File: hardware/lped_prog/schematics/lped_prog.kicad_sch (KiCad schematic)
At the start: 12 parts, among them J1 J-Link Header, J2 Conn_01x01_Pin, J3 Conn_01x01_Pin, J4 Conn_01x01_Pin, J5 Conn_01x01_Pin, J6 Conn_01x01_Pin, J7 Conn_01x01_Pin

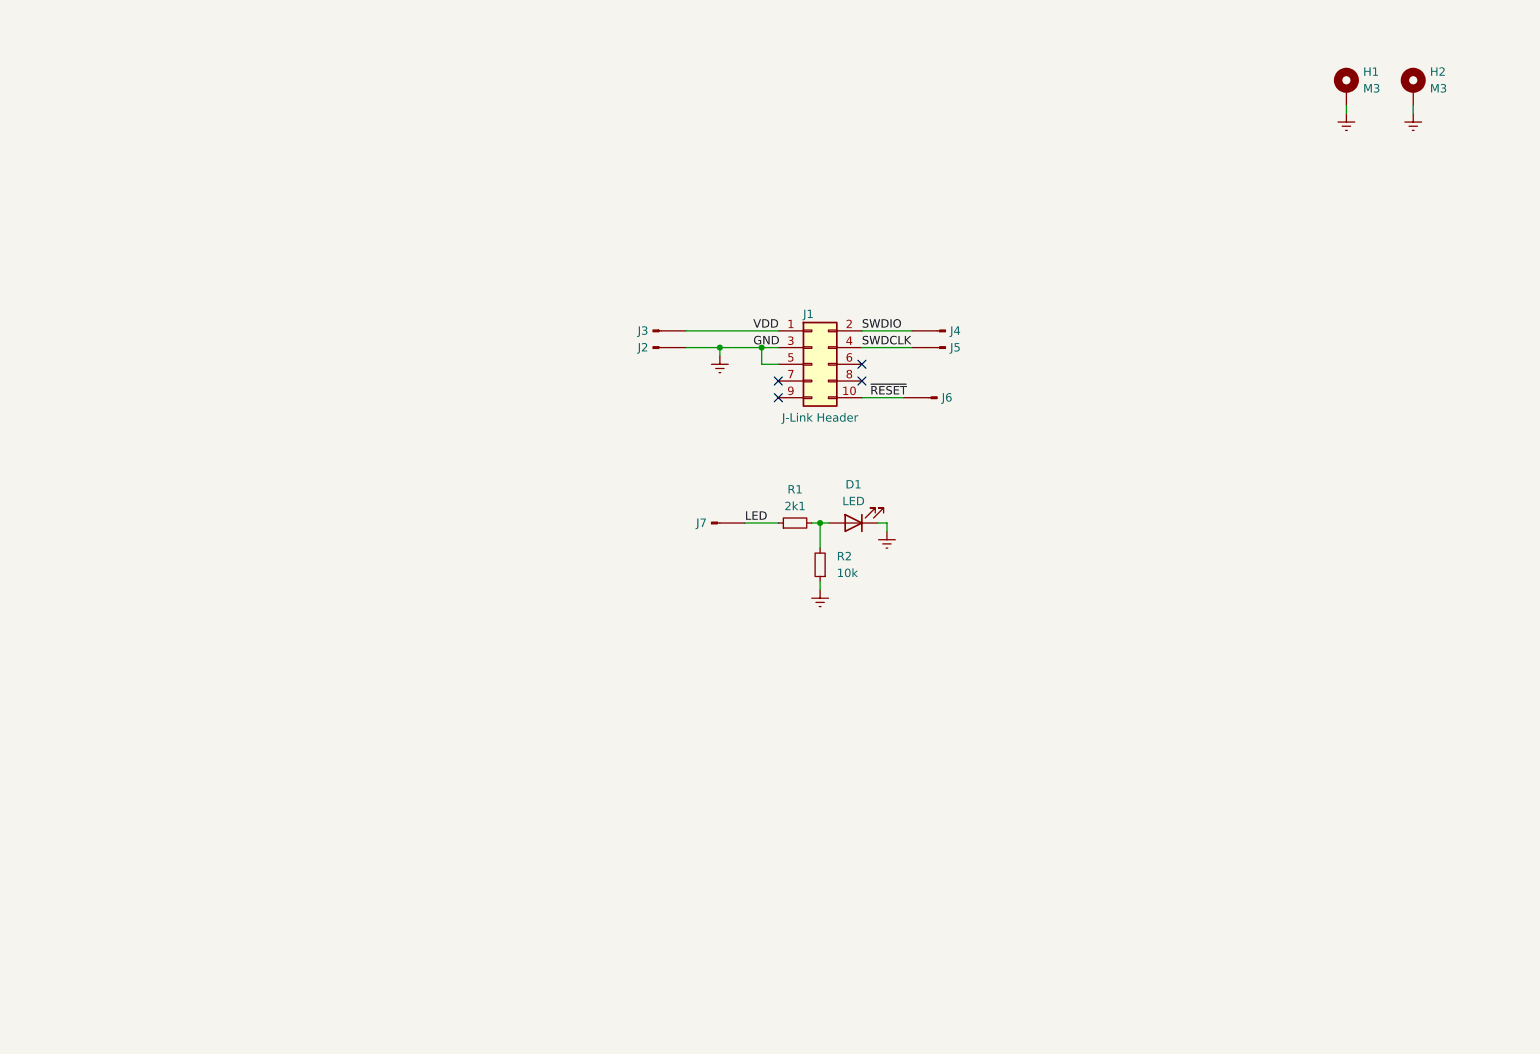
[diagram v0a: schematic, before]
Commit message: feat(hardware): added usb and manual input to programmer, added reset button and connection switch
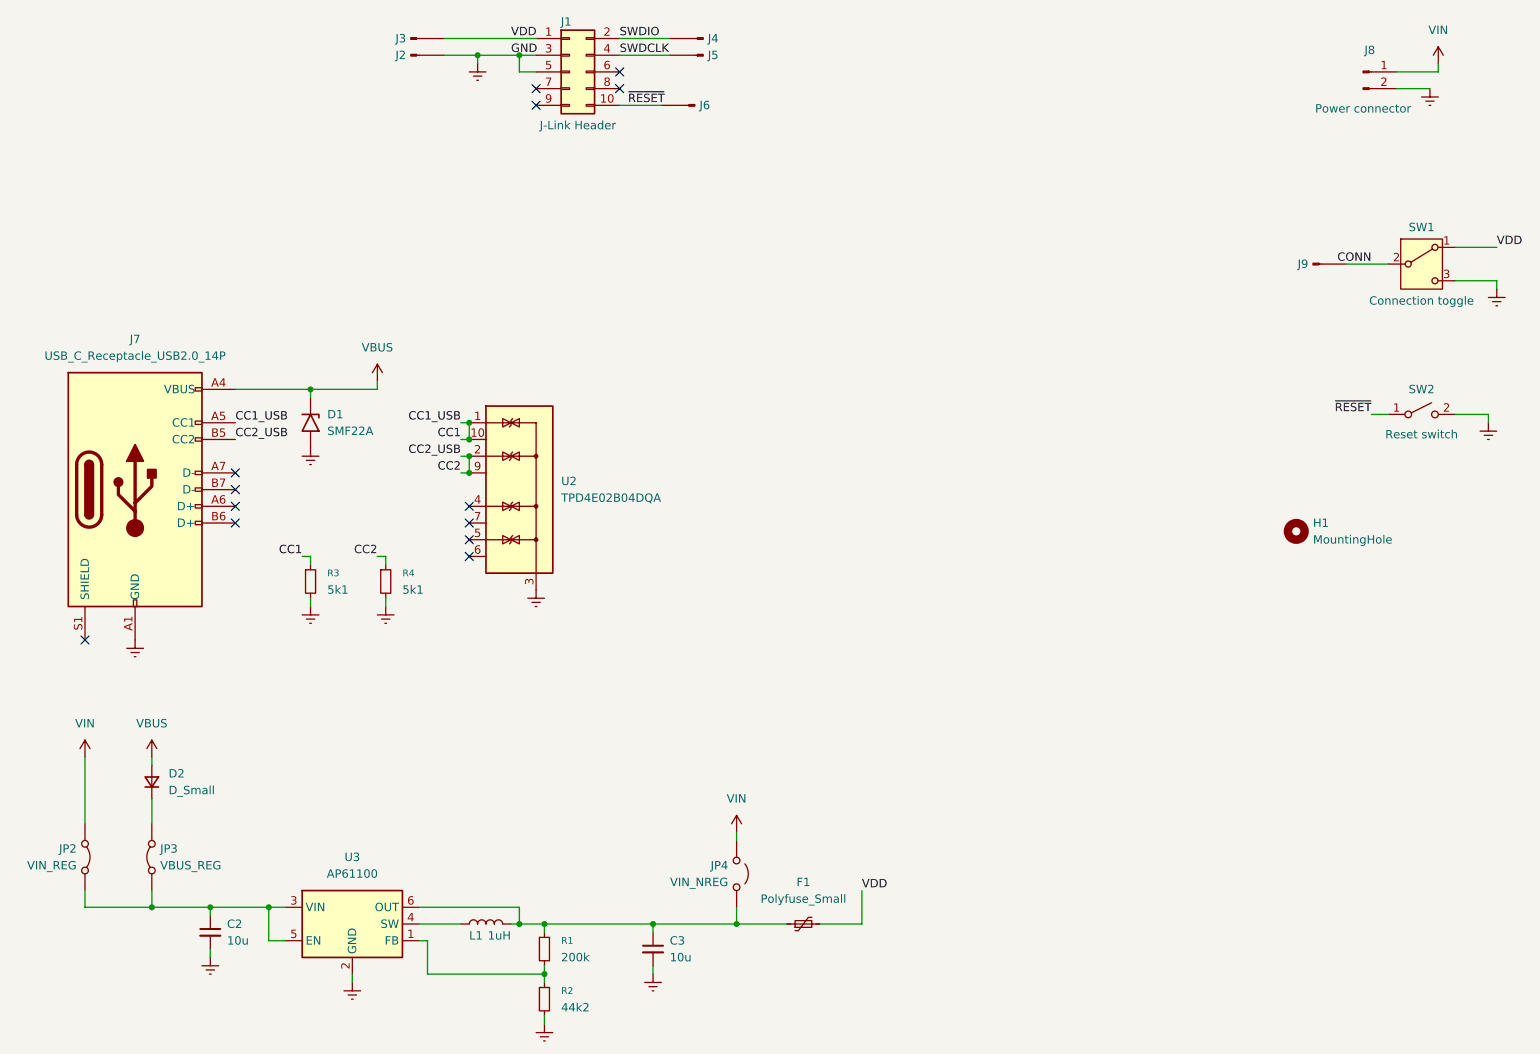
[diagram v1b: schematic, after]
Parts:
- removed D1: LED, Diode_SMD:D_0805_2012Metric, symbol Device:LED
- removed H1, H2: M3, MountingHole:MountingHole_2.7mm_M2.5_ISO7380_Pad, symbol Mechanical:MountingHole_Pad
- removed J7: Conn_01x01_Pin, Connector_Pin:Pin_D0.9mm_L10.0mm_W2.4mm_FlatFork, symbol Connector:Conn_01x01_Pin
- added C2, C3: 10u, Capacitor_SMD:C_0603_1608Metric, symbol Device:C_Small
- added D1: SMF22A, Diode_SMD:D_SMF, symbol Diode:SMF22A
- added D2: D_Small, Diode_SMD:D_0402_1005Metric, symbol Device:D_Small
- added F1: Polyfuse_Small, Fuse:Fuse_1206_3216Metric, symbol Device:Polyfuse_Small
- added H1: MountingHole, MountingHole:MountingHole_3.2mm_M3, symbol Mechanical:MountingHole
- added J7: USB_C_Receptacle_USB2.0_14P, Connector_USB:USB_C_Receptacle_GCT_USB4105-xx-A_16P_TopMnt_Horizontal, symbol Connector:USB_C_Receptacle_USB2.0_14P
- added J8: Power connector, Connector_PinHeader_2.54mm:PinHeader_1x02_P2.54mm_Vertical, symbol Connector:Conn_01x02_Pin
- added J9: Conn_01x01_Pin, Connector_Pin:Pin_D0.9mm_L10.0mm_W2.4mm_FlatFork, symbol Connector:Conn_01x01_Pin
- added JP2: VIN_REG, Connector_PinHeader_2.54mm:PinHeader_1x02_P2.54mm_Vertical, symbol Jumper:Jumper_2_Bridged
- added JP3: VBUS_REG, Connector_PinHeader_2.54mm:PinHeader_1x02_P2.54mm_Vertical, symbol Jumper:Jumper_2_Bridged
- added JP4: VIN_NREG, Connector_PinHeader_2.54mm:PinHeader_1x02_P2.54mm_Vertical, symbol Jumper:Jumper_2_Open
- added L1: 1uH, Inductor_SMD:L_0805_2012Metric, symbol Device:L
- added R3, R4: 5k1, Resistor_SMD:R_0402_1005Metric, symbol Device:R_Small
- added SW1: Connection toggle, Switches_Toggles:EG1215AA, symbol Switch:SW_SPDT
- added SW2: Reset switch, Button_Switch_THT:SW_PUSH_6mm_H4.3mm, symbol Switch:SW_SPST
- added U2: TPD4E02B04DQA, Package_SON:USON-10_2.5x1.0mm_P0.5mm, symbol Power_Protection:TPD4E02B04DQA
- added U3: AP61100, Package_TO_SOT_SMD:SOT-563, symbol Regulator_Switching:AP61300Z6
- R1: value 2k1 -> 200k
- R2: value 10k -> 44k2
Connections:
- net Earth: now also R2.2, C2.2, C3.2, D1.2 (A2), J7.A1 (GND), J7.A12 (GND), J7.B1 (GND), J7.B12 (GND), J8.2 (Pin_2), R3.2, R4.2, SW1.3 (C), SW2.2 (B), U2.3 (G), U2.8 (G), U3.2 (GND); no longer R2.1
- net VDD: now also F1.2, SW1.1 (A)
- net ~{RESET}: now also SW2.1 (A)
- net at R1.2: now also R2.1, U3.1 (FB); no longer R2.2
- net LED: no longer names the net of R1.1
- net LED: now also C3.1, F1.1, JP4.1 (A), L1.2, U3.6 (OUT)
- new net: C2.1, JP2.1 (A), JP3.1 (A), U3.3 (VIN), U3.5 (EN)
- new net: D2.1 (K), JP3.2 (B)
- new net: L1.1, U3.4 (SW)
- new net CC1: J7.A5 (CC1), R3.1, U2.1 (IO1), U2.10 (NC)
- new net CC2: J7.B5 (CC2), R4.1, U2.2 (IO2), U2.9 (NC)
- new net CONN: J9.1 (Pin_1), SW1.2 (B)
- new net VBUS: D1.1 (A1), D2.2 (A), J7.A4 (VBUS), J7.A9 (VBUS), J7.B4 (VBUS), J7.B9 (VBUS)
- new net VIN: J8.1 (Pin_1), JP2.2 (B), JP4.2 (B)
- no-connect marks 4 -> 13
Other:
- moved on the sheet: J1, J2, J3, J4, J5, J6

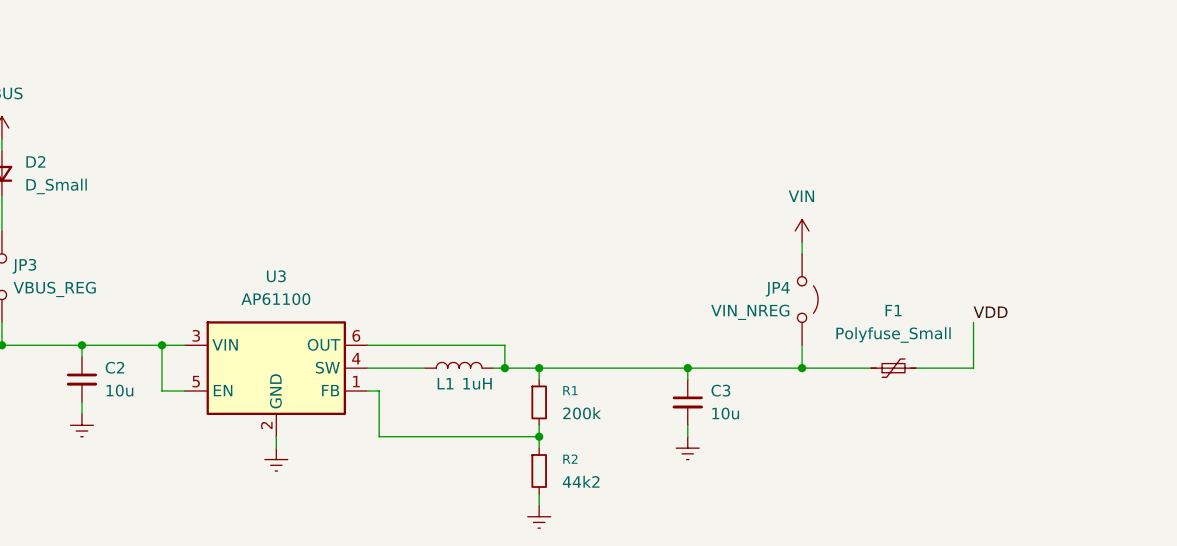
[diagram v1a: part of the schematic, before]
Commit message: feat(hardware): chaged regulator
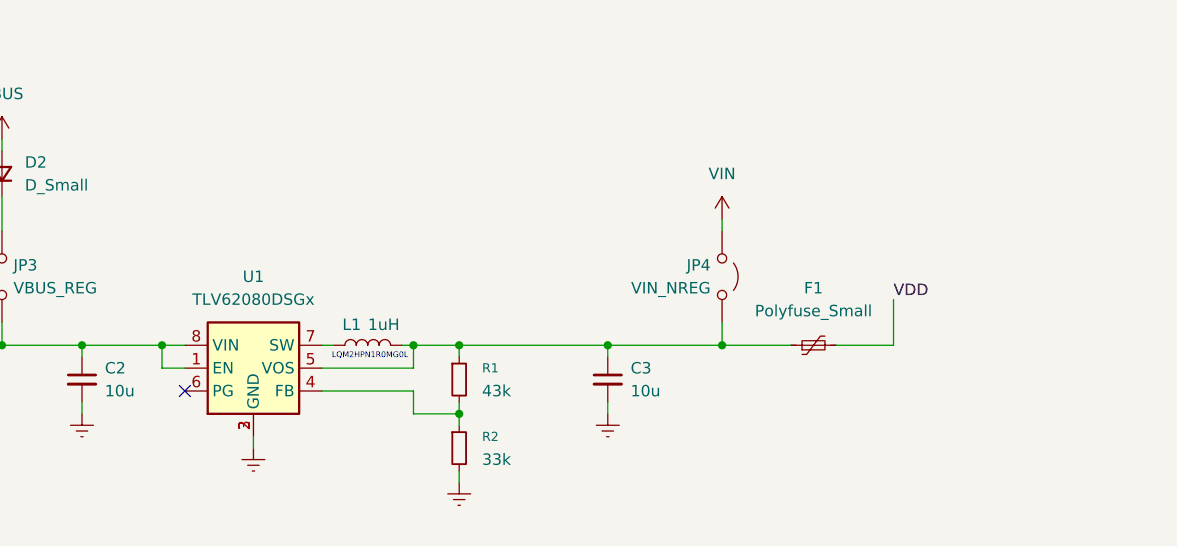
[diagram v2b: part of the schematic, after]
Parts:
- removed U3: AP61100, Package_TO_SOT_SMD:SOT-563, symbol Regulator_Switching:AP61300Z6
- added U1: TLV62080DSGx, Package_SON:WSON-8-1EP_2x2mm_P0.5mm_EP0.9x1.6mm, symbol Regulator_Switching:TLV62080DSGx
- L1: footprint Inductor_SMD:L_0805_2012Metric -> Inductor_SMD:L_1008_2520Metric
- R1: value 200k -> 43k
- R2: value 44k2 -> 33k
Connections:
- net Earth: now also U1.2 (GND), U1.3 (GND), U1.9 (GND)
- net at C3.1, F1.1, JP4.1 (A)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: now also U1.5 (VOS)
- net at R1.2, R2.1: now also U1.4 (FB)
- net at C2.1, JP2.1 (A), JP3.1 (A): now also U1.1 (EN), U1.8 (VIN)
- net at L1.1: now also U1.7 (SW)
- no-connect marks 13 -> 14
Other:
- note added: "LQM2HPN1R0MG0L"
- moved on the sheet: C3, F1, JP4, L1, R1, R2

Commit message: fix(hardware): minor fixes before manufacturing
Changed footprint of USB protection diode
Changed footprint of Programmer fuse
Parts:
- D2: footprint Diode_SMD:D_0402_1005Metric -> Diode_SMD:D_SOD-123F
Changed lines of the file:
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@@
 			)
 		)
-		(property "Footprint" "Diode_SMD:D_0402_1005Metric"
+		(property "Footprint" "Diode_SMD:D_SOD-123F"
 			(at 48.26 148.59 90)
 			(effects
